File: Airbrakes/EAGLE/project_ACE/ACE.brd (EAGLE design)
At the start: 1 part

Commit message: Update CAD with BNO08x, OpenLog
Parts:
- removed SV1: (no value), con-lstb:MA03-2
- added J2, J4: SMD, SparkFun-Connectors:1X04_1MM_RA
- added J3: PTH, SparkX:1X04_NO_SILK
- added J6: (no value), SparkFun-Connectors:1X06_NO_SILK
- added JP1, JP2: (no value), microbuilder:1X06_ROUND_70
- added PORTENTA_H7: ABX00042, ABX00042:MODULE_ABX00042
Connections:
- new net 3.3V: J2.2, J3.2, J4.2, J6.3, JP1.2
- new net BOOT: JP2.1
- new net CS: JP2.6
- new net DTR: J6.6
- new net GND: J2.1, J3.1, J4.1, J6.1, J6.2, JP1.3, PORTENTA_H7.J1_22, PORTENTA_H7.J1_31, PORTENTA_H7.J1_42, PORTENTA_H7.J1_47, PORTENTA_H7.J1_54
- new net GND_1: PORTENTA_H7.J2_24, PORTENTA_H7.J2_33, PORTENTA_H7.J2_44, PORTENTA_H7.J2_57, PORTENTA_H7.J2_70
- new net INT: JP1.6
- new net MOSI: JP2.5
- new net PS0: JP2.2
- new net PS1: JP2.3
- new net RST: JP2.4
- new net RXI: J6.4
- new net SCL: J2.4, J3.4, J4.4
- new net SCL/SCK/RX: JP1.4
- new net SDA: J2.3, J3.3, J4.3
- new net SDA/MISO/TX: JP1.5
- new net TXO: J6.5
- new net USB1_VBUS: PORTENTA_H7.J1_23
- new net V-SDCARD: PORTENTA_H7.J1_72
- new net VCC: JP1.1, PORTENTA_H7.J2_34
- new net VCC/+3V3: PORTENTA_H7.J2_23, PORTENTA_H7.J2_43, PORTENTA_H7.J2_69
- new net VSYS: PORTENTA_H7.J1_53, PORTENTA_H7.J1_64

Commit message: Fix version
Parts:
- added U$1: MIKROE-ALTITUDE-6-CLICK-DVC, MIKROE-4903:MIKROE-ALTITUDE-6-CLICK-PINOUT
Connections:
- removed net SCL/SCK/RX: JP1.4
- removed net SDA/MISO/TX: JP1.5
- net GND: now also U$1.GND_0, U$1.GND_1
- net SCL: now also JP1.4, U$1.SCL
- net SDA: now also JP1.5, U$1.SDA
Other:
- board outline added: 27.9 x 26.7 mm
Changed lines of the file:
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@@
 <board>
 <plain>
-<text x="2.54" y="6.35" size="1.778" layer="1">ACE LAYOUT</text>
+<text x="2.54" y="-11.43" size="1.778" layer="1">ACE LAYOUT</text>
 </plain>
 <attributes>
@@
 <attribute name="VALUE" x="-24.13" y="-26.162" size="0.6096" layer="27" font="vector" ratio="20"/>
 </element>
+<element name="U$1" library="MIKROE-4903" package="MIKROE-ALTITUDE-6-CLICK-PINOUT" value="MIKROE-ALTITUDE-6-CLICK-DVC" x="-53.34" y="-20.32" smashed="yes"/>
 </elements>
 <signals>
@@
 <contactref element="J2" pad="1"/>
 <contactref element="J4" pad="1"/>
-<wire x1="-13.23" y1="59.33" x2="-10.03" y2="59.33" width="0" layer="19" extent="1-1"/>
+<contactref element="U$1" pad="GND_0"/>
+<contactref element="U$1" pad="GND_1"/>
+<wire x1="-27.94" y1="-15.24" x2="-50.8" y2="-15.24" width="0" layer="19" extent="1-1"/>
+<wire x1="-22.86" y1="-19.05" x2="-27.94" y2="-15.24" width="0" layer="19" extent="1-1"/>
+<wire x1="-22.86" y1="-24.13" x2="-22.86" y2="-19.05" width="0" layer="19" extent="1-1"/>
+<wire x1="-20.32" y1="-24.13" x2="-22.86" y2="-24.13" width="0" layer="19" extent="1-1"/>
+<wire x1="-21.82" y1="-11.43" x2="-27.94" y2="-15.24" width="0" layer="19" extent="1-1"/>
+<wire x1="-21.82" y1="-5.08" x2="-21.82" y2="-11.43" width="0" layer="19" extent="1-1"/>
+<wire x1="-16.51" y1="2.54" x2="-21.82" y2="-5.08" width="0" layer="19" extent="1-1"/>
+<wire x1="-15.23" y1="56.25" x2="-16.51" y2="2.54" width="0" layer="19" extent="1-1"/>
+<wire x1="-13.23" y1="59.33" x2="-15.23" y2="56.25" width="0" layer="19" extent="1-1"/>
+<wire x1="-10.03" y1="59.33" x2="-13.23" y2="59.33" width="0" layer="19" extent="1-1"/>
 <wire x1="-8.83" y1="56.25" x2="-10.03" y2="59.33" width="0" layer="19" extent="1-1"/>
 <wire x1="-11.23" y1="56.25" x2="-8.83" y2="56.25" width="0" layer="19" extent="1-1"/>
-<wire x1="-15.23" y1="56.25" x2="-13.23" y2="59.33" width="0" layer="19" extent="1-1"/>
-<wire x1="-16.51" y1="2.54" x2="-15.23" y2="56.25" width="0" layer="19" extent="1-1"/>
-<wire x1="-21.82" y1="-5.08" x2="-16.51" y2="2.54" width="0" layer="19" extent="1-1"/>
-<wire x1="-21.82" y1="-11.43" x2="-21.82" y2="-5.08" width="0" layer="19" extent="1-1"/>
-<wire x1="-22.86" y1="-19.05" x2="-21.82" y2="-11.43" width="0" layer="19" extent="1-1"/>
-<wire x1="-22.86" y1="-24.13" x2="-22.86" y2="-19.05" width="0" layer="19" extent="1-1"/>
-<wire x1="-20.32" y1="-24.13" x2="-22.86" y2="-24.13" width="0" layer="19" extent="1-1"/>
 </signal>
 <signal name="VSYS">
@@
 <wire x1="-10.03" y1="16.15" x2="-21.59" y2="2.54" width="0" layer="19" extent="1-1"/>
 </signal>
-<signal name="SCL/SCK/RX">
-<contactref element="JP1" pad="4"/>
-</signal>
-<signal name="SDA/MISO/TX">
-<contactref element="JP1" pad="5"/>
-</signal>
 <signal name="3.3V" class="2">
 <contactref element="JP1" pad="2"/>
@@
 <contactref element="J3" pad="4"/>
 <contactref element="J4" pad="4"/>
-<wire x1="-18.82" y1="-11.43" x2="-15.24" y2="-19.05" width="0" layer="19" extent="1-1"/>
-<wire x1="-18.82" y1="-5.08" x2="-18.82" y2="-11.43" width="0" layer="19" extent="1-1"/>
+<contactref element="JP1" pad="4"/>
+<contactref element="U$1" pad="SCL"/>
+<wire x1="-18.82" y1="-5.08" x2="-50.8" y2="-7.62" width="0" layer="19" extent="1-1"/>
+<wire x1="-18.82" y1="-11.43" x2="-18.82" y2="-5.08" width="0" layer="19" extent="1-1"/>
+<wire x1="-15.24" y1="-19.05" x2="-18.82" y2="-11.43" width="0" layer="19" extent="1-1"/>
+<wire x1="-13.97" y1="2.54" x2="-18.82" y2="-5.08" width="0" layer="19" extent="1-1"/>
 </signal>
 <signal name="SDA">
@@
 <contactref element="J3" pad="3"/>
 <contactref element="J4" pad="3"/>
-<wire x1="-19.82" y1="-11.43" x2="-17.78" y2="-19.05" width="0" layer="19" extent="1-1"/>
+<contactref element="JP1" pad="5"/>
+<contactref element="U$1" pad="SDA"/>
+<wire x1="-19.82" y1="-11.43" x2="-50.8" y2="-10.16" width="0" layer="19" extent="1-1"/>
 <wire x1="-19.82" y1="-5.08" x2="-19.82" y2="-11.43" width="0" layer="19" extent="1-1"/>
+<wire x1="-17.78" y1="-19.05" x2="-19.82" y2="-11.43" width="0" layer="19" extent="1-1"/>
+<wire x1="-11.43" y1="2.54" x2="-19.82" y2="-5.08" width="0" layer="19" extent="1-1"/>
 </signal>
 </signals>

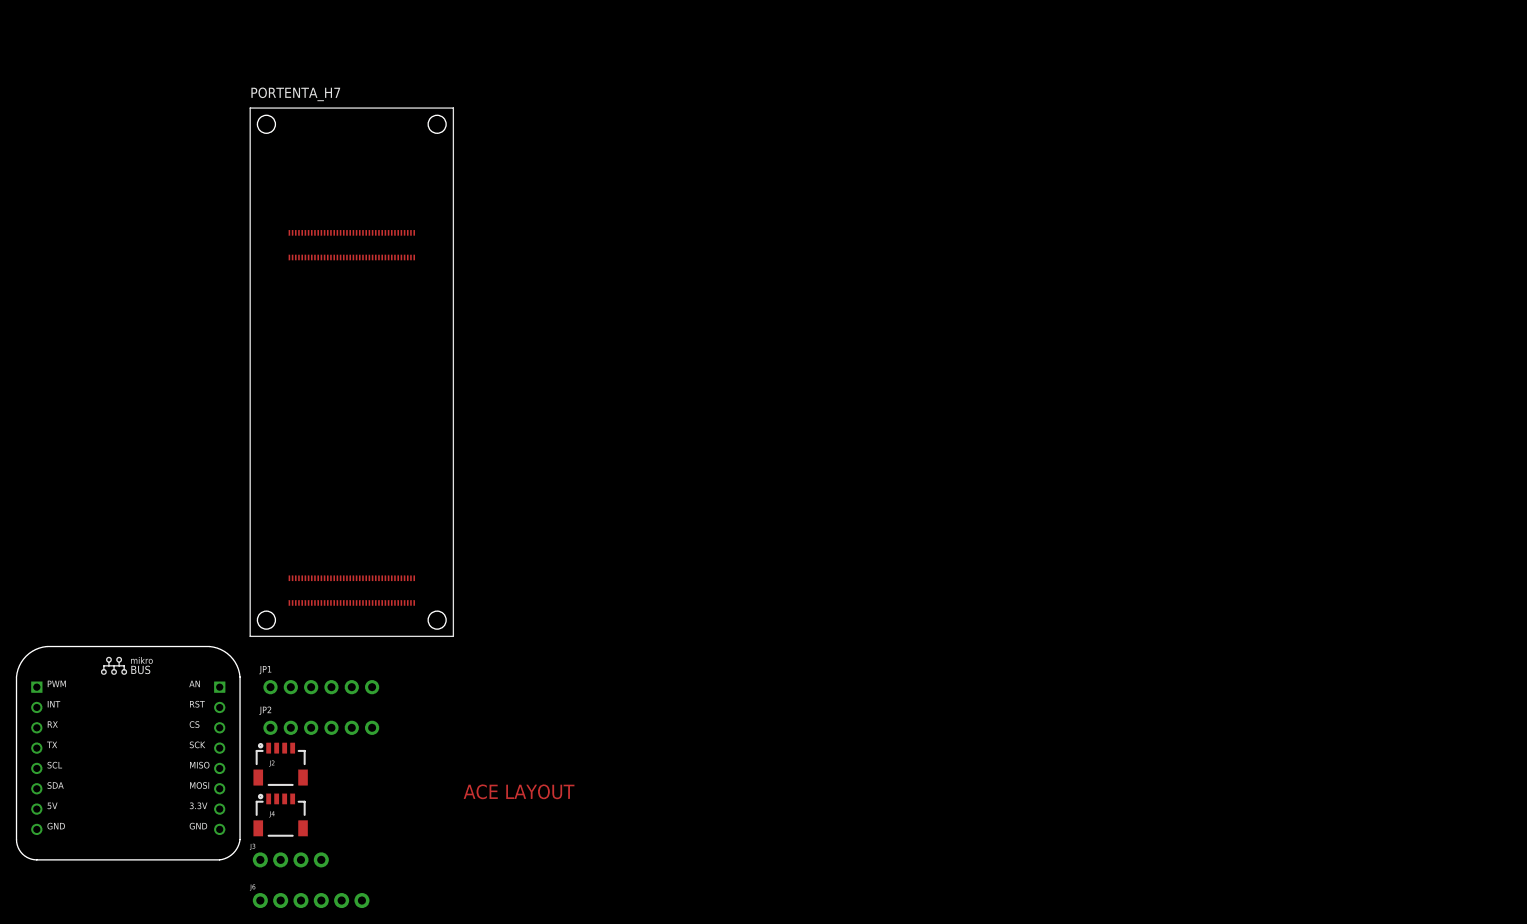
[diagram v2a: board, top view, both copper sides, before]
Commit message: Update CAD with BNO08x footprint
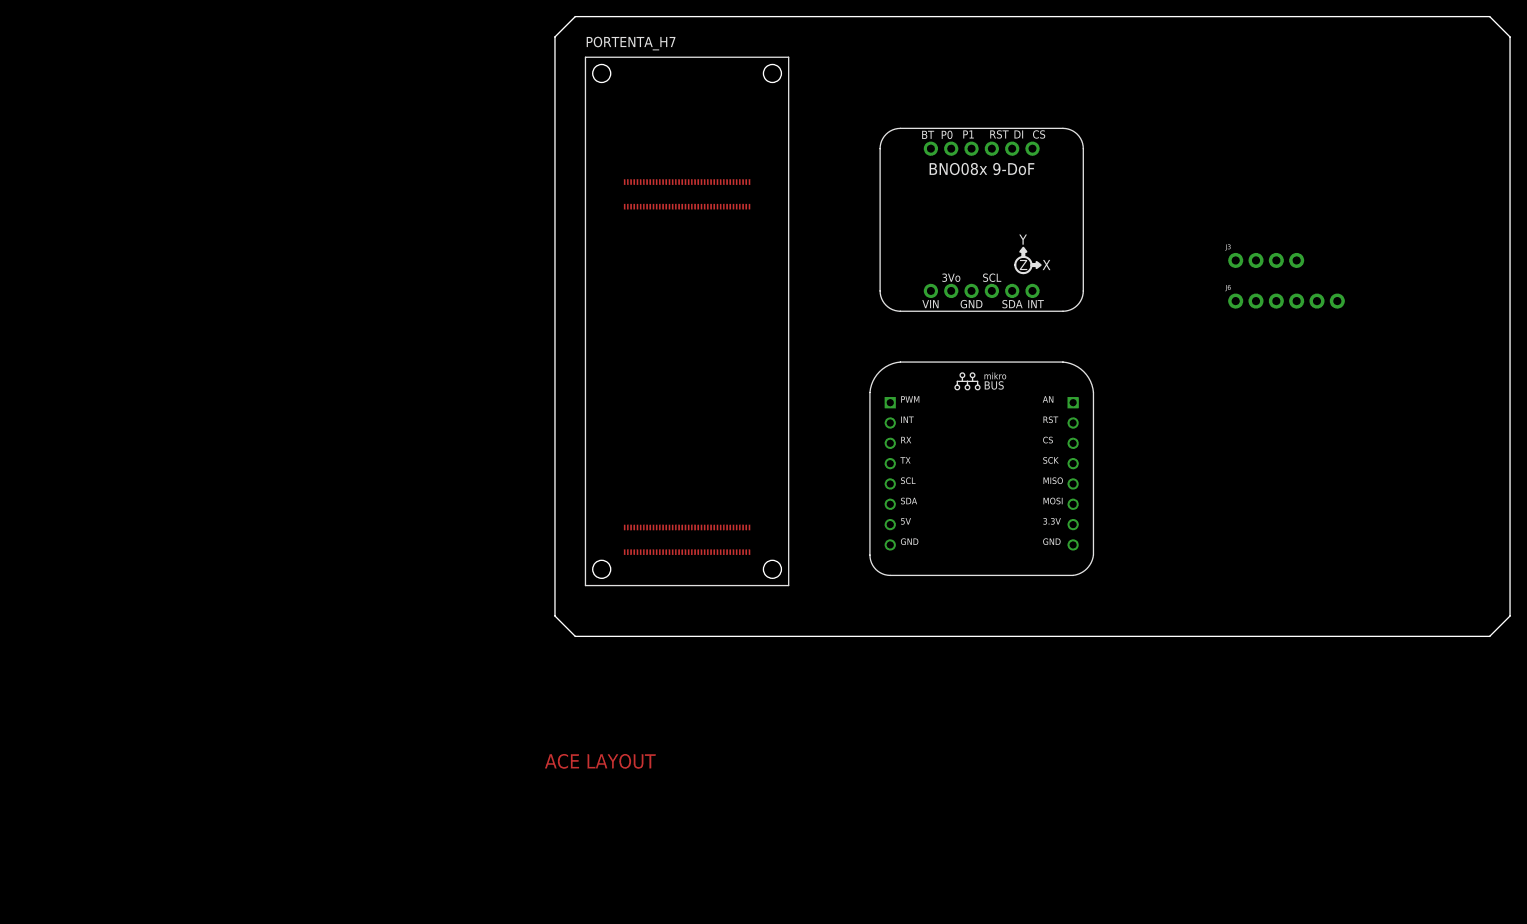
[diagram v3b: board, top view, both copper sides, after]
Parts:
- removed J2, J4: SMD, SparkFun-Connectors:1X04_1MM_RA
- removed JP1, JP2: (no value), microbuilder:1X06_ROUND_70
- added U$5: ADAFRUIT_BNO08X, ADAFRUIT_BNO08x:ADAFRUIT_BNO08X_FOOTPRINT
- moved J3 143.1 mm to (99.1, 55.9)
- moved J6 143.1 mm to (99.1, 50.8)
- moved U$1 112.5 mm to (53.3, 15.2)
- moved PORTENTA_H7 42.4 mm to (30.5, 48.3)
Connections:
- removed net BOOT: JP2.1
- removed net CS: JP2.6
- removed net INT: JP1.6
- removed net MOSI: JP2.5
- removed net PS0: JP2.2
- removed net PS1: JP2.3
- removed net RST: JP2.4
- new net N$1: U$1.GND_1
- net 3.3V: no longer J2.2, J4.2, JP1.2
- net GND: now also U$5.SCL; no longer J2.1, J4.1, JP1.3, U$1.GND_1
- net SCL: no longer J2.4, J4.4, JP1.4
- net SDA: no longer J2.3, J4.3, JP1.5
- net VCC: no longer JP1.1
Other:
- board size 27.9 x 26.7 mm -> 119.4 x 77.5 mm

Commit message: Reorganize board layout and fix nets
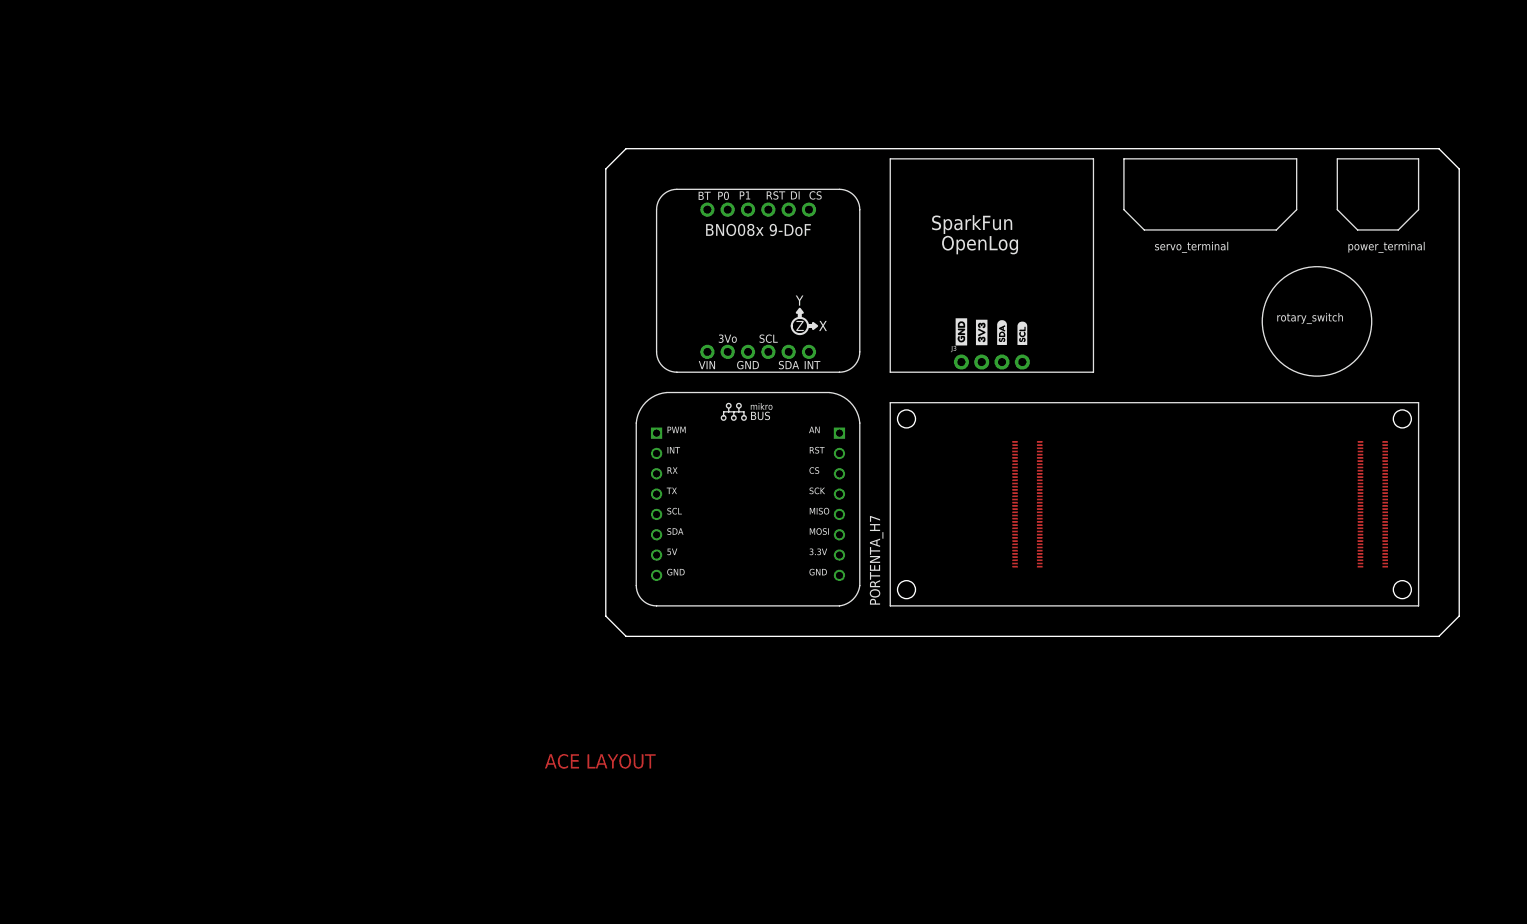
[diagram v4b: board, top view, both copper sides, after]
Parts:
- removed J6: (no value), SparkFun-Connectors:1X06_NO_SILK
- added U$16: (no value), buzzard_labels (13):SDA1
- added U$19: (no value), buzzard_labels (13):SCL2
- added U$8: (no value), Labels:3V3-03
- added U$9: (no value), Labels:GND-03
- moved PORTENTA_H7 62.7 mm to (88.9, 25.4), turned to 90 degrees
- moved J3 36.6 mm to (64.8, 43.2)
- moved U$1 29.5 mm to (24.1, 11.4)
- moved U$5 29.0 mm to (25.4, 40.6)
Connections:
- removed net DTR: J6.6
- removed net RXI: J6.4
- removed net TXO: J6.5
- net 3.3V: now also U$1.3.3V, U$5.3VO; no longer J6.3
- net GND: now also U$5.GND; no longer J6.1, J6.2, U$5.SCL
- net SCL: now also U$5.SCL
- net SDA: now also U$5.SDA
- net VCC: now also U$1.5V, U$5.VIN
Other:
- board size 119.4 x 77.5 mm -> 106.7 x 61 mm
- board text added: "OpenLog"
- board text added: "SparkFun"
- board text added: "power_terminal"
- board text added: "rotary_switch"
- board text added: "servo_terminal"
